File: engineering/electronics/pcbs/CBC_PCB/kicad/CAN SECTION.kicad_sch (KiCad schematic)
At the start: 44 parts, among them U25 ADM3053BRWZ-REEL7, U26 ADM3053BRWZ-REEL7, X1 16MHz, X2 16MHz

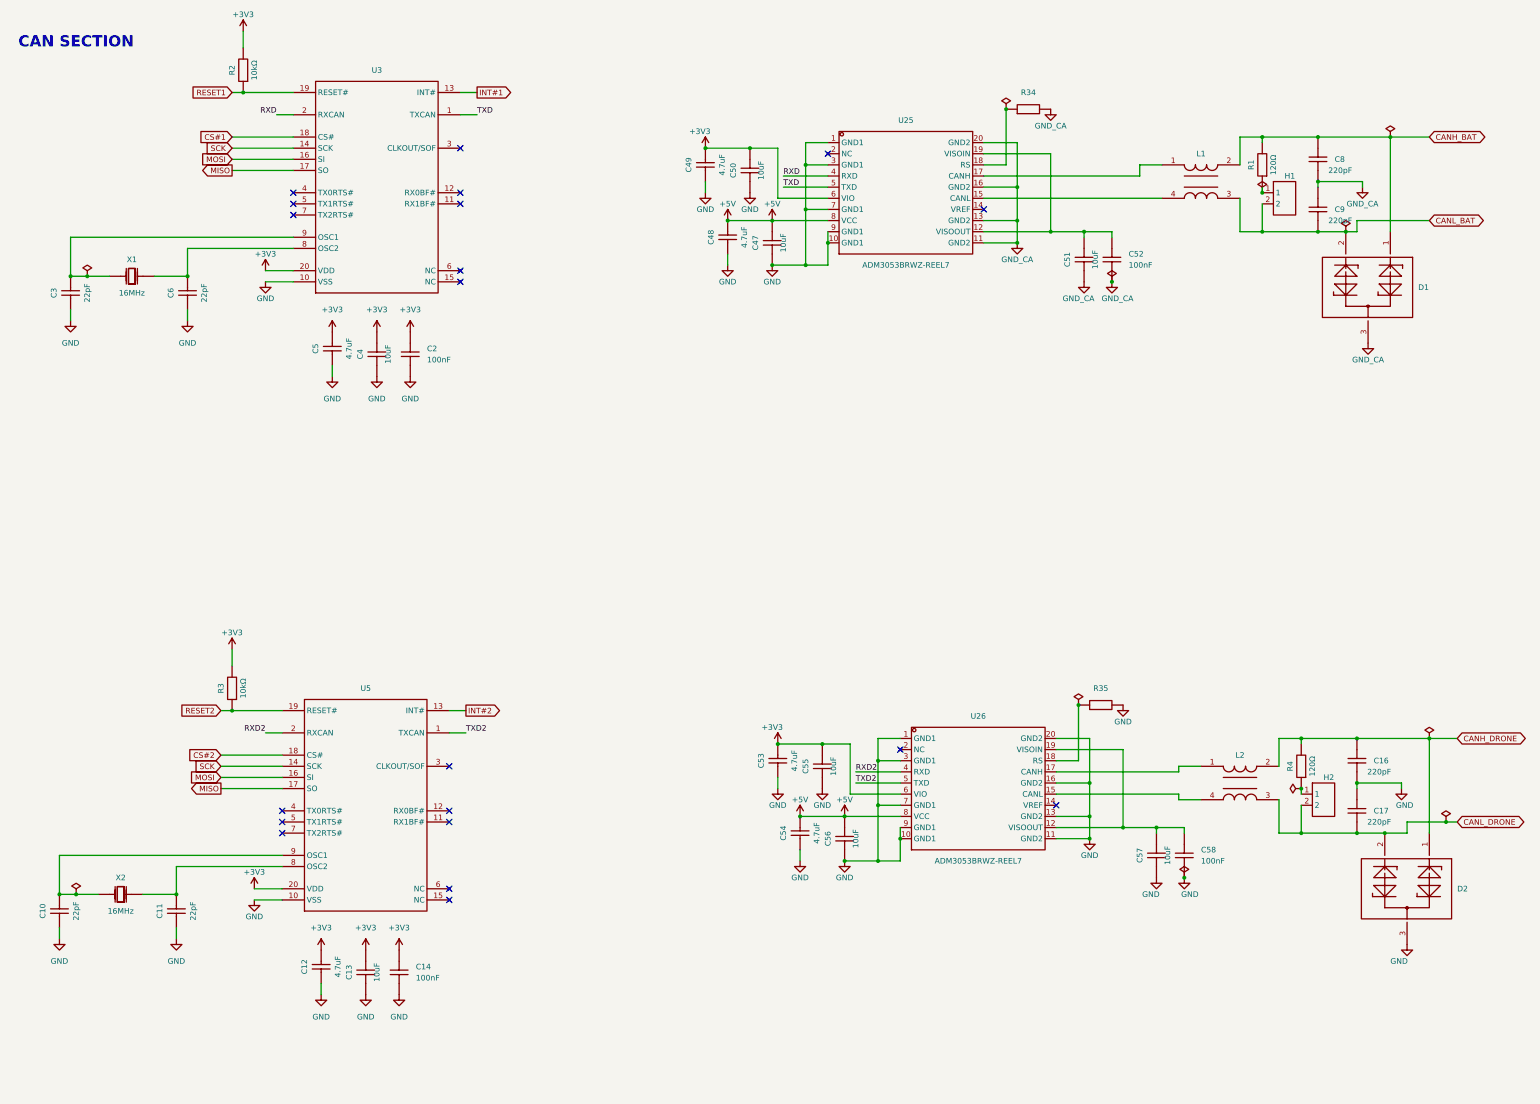
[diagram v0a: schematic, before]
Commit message: fix(cbc): integrate ordered PCB update
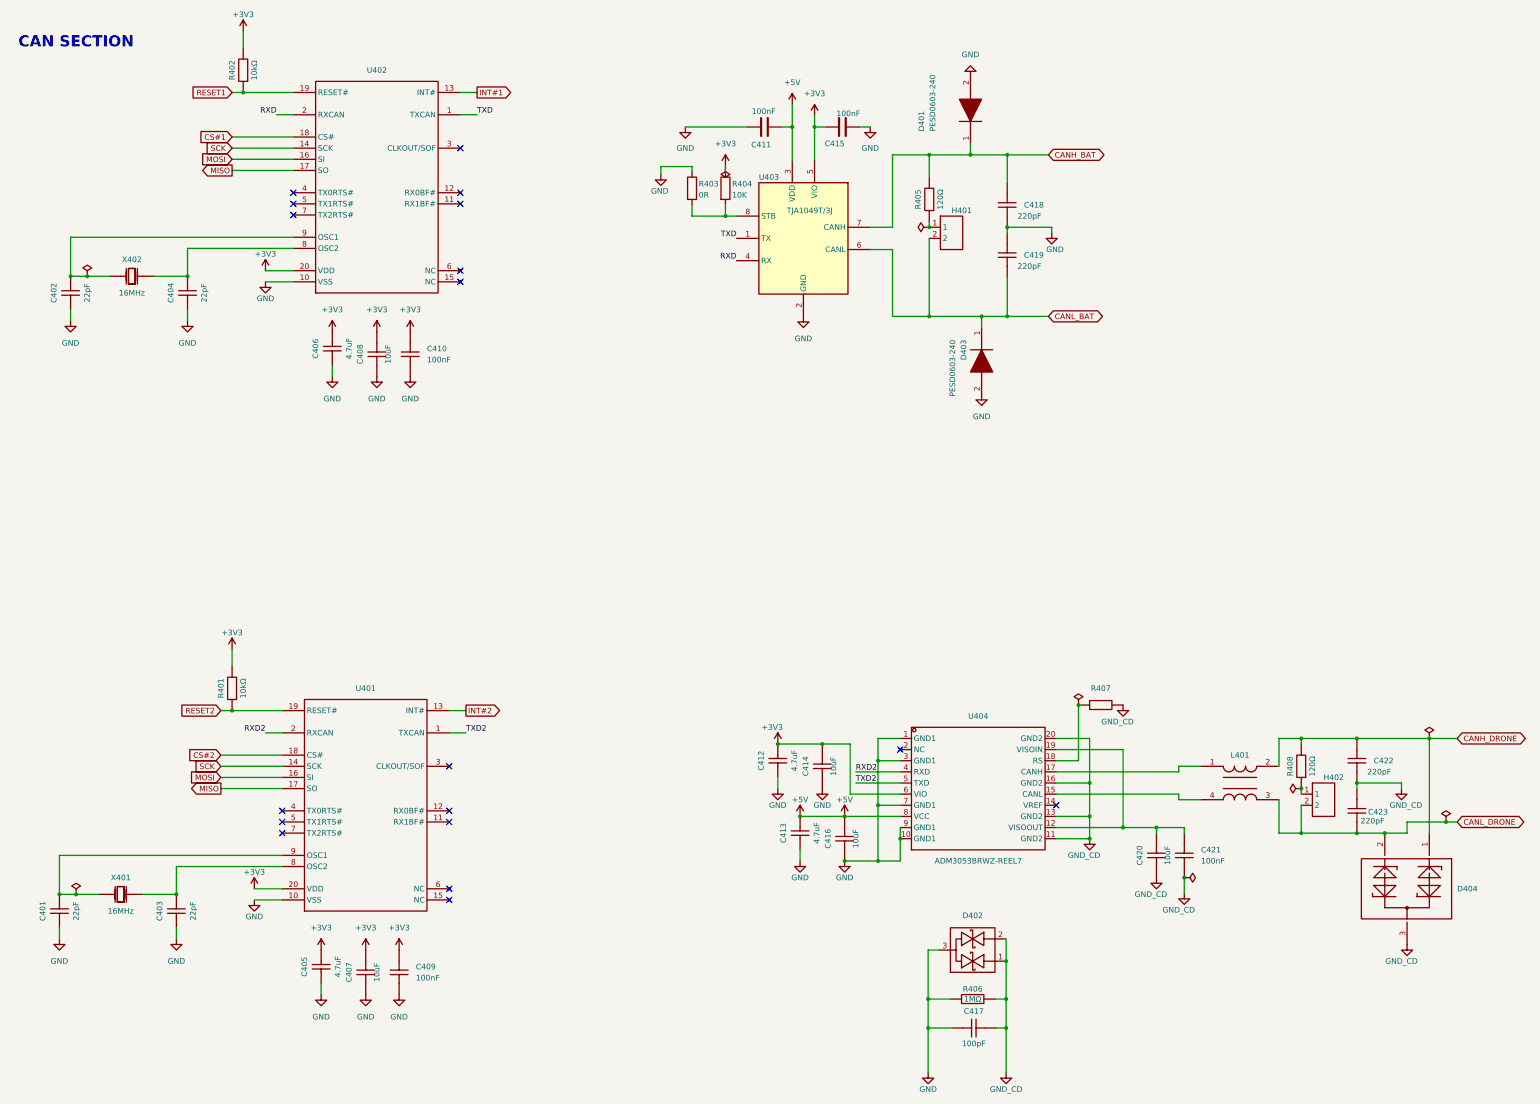
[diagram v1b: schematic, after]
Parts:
- removed C47, C50, C51: 10uF, EasyEDA_Lib:C0805, symbol CBC_PCB:GRM21BR61H106KE43L
- removed C48, C49: 4.7uF, EasyEDA_Lib:C0805, symbol CBC_PCB:CL21A475KBQNNNE
- removed C52: 100nF, EasyEDA_Lib:C0402, symbol CBC_PCB:CC0402KRX7R7BB104
- removed D1: (no value), EasyEDA_Lib:SOT-23-3_L2.9-W1.3-P1.90-LS2.4-BL-2, symbol CBC_PCB:NUP2105LT1G
- removed L1: (no value), EasyEDA_Lib:FILTER-SMD_4P-L4.5-W3.2_ACT45B-510-2P, symbol CBC_PCB:ACT45B-510-2P-TF
- removed R34: 0Ω, EasyEDA_Lib:R0402, symbol CBC_PCB:RC0402FR-070RL
- removed U25: ADM3053BRWZ-REEL7, EasyEDA_Lib:SOIC-20_L13.0-W7.6-P1.27-LS10.3-BL, symbol CBC_PCB:ADM3053BRWZ-REEL7
- added C411, C415: 100nF, Capacitor_SMD:C_0805_2012Metric_Pad1.18x1.45mm_HandSolder, symbol Device:C
- added C417: 100pF, EasyEDA_Lib_2:C0805, symbol EasyEDA_Lib_2:C0805C101J2GAC7800
- added D401, D403: PESD0603-240, Samacsys:DIONC1608X55N, symbol Samacsys_kicad_sym:PESD0603-240
- added D402: (no value), EasyEDA_Lib_2:SOT-323-3_L2.0-W1.3-P1.30-LS2.1-BR, symbol EasyEDA_Lib_2:PESD1CAN-UX
- added R403: 0R, Resistor_SMD:R_0805_2012Metric_Pad1.20x1.40mm_HandSolder, symbol Device:R
- added R404: 10K, Resistor_SMD:R_0805_2012Metric_Pad1.20x1.40mm_HandSolder, symbol Device:R
- added R406: 1MΩ, EasyEDA_Lib_2:R0805, symbol EasyEDA_Lib_2:RC0805FR-071ML
- added U403: TJA1049T/3J, Samacsys:SOIC127P600X175-8N, symbol Samacsys_kicad_sym:TJA1049T_3J
- renumbered C10 to C401, C3 to C402, C11 to C403, C6 to C404, C12 to C405, C5 to C406, C13 to C407, C4 to C408, C14 to C409, C2 to C410, C53 to C412, C54 to C413, C55 to C414, C56 to C416, C8 to C418, C9 to C419, C57 to C420, C58 to C421, C16 to C422, C17 to C423, D2 to D404, H1 to H401, H2 to H402, L2 to L401, R3 to R401, R2 to R402, R1 to R405, R35 to R407, R4 to R408, U5 to U401, U3 to U402, U26 to U404, X2 to X401, X1 to X402
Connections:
- net GND_CA is gone; now on net GND: C418.1, C419.2
- net +3V3: now also C415.1, R404.1, U403.5 (VIO)
- net +5V: now also C411.2, U403.3 (VDD)
- net CANH_BAT: now also D401.1 (K), U403.7 (CANH)
- net CANL_BAT: now also D403.1 (K), U403.6 (CANL)
- net GND: now also C411.1, C415.2, C417.1, D401.2 (A), D402.3, D403.2 (A), R403.1, R406.1, U403.2 (GND); no longer C420.1, C421.1, C422.1, C423.2, D404.3, R407.2, U404.11 (GND2), U404.13 (GND2), U404.16 (GND2), U404.20 (GND2)
- net RXD: now also U403.4 (RX)
- net TXD: now also U403.1 (TX)
- new net: R403.2, R404.2, U403.8 (STB)
- new net GND_CD: C417.2, C420.1, C421.1, C422.1, C423.2, D402.1, D402.2, D404.3, R406.2, R407.2, U404.11 (GND2), U404.13 (GND2), U404.16 (GND2), U404.20 (GND2)
- no-connect marks 20 -> 18
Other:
- moved on the sheet: C418, C419, H401, R405
